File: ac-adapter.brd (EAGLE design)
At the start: 113 x 52.7 mm, 88 parts, among them IC1 SSC3S900, IC2 TL431, Q1 300V 5A, Q2 300V 5A, Q3 TLP621-1, T1 COMMON_FILTER-SU10VFC, T2 TRANSFORMAER_FLYBACK-ETD34

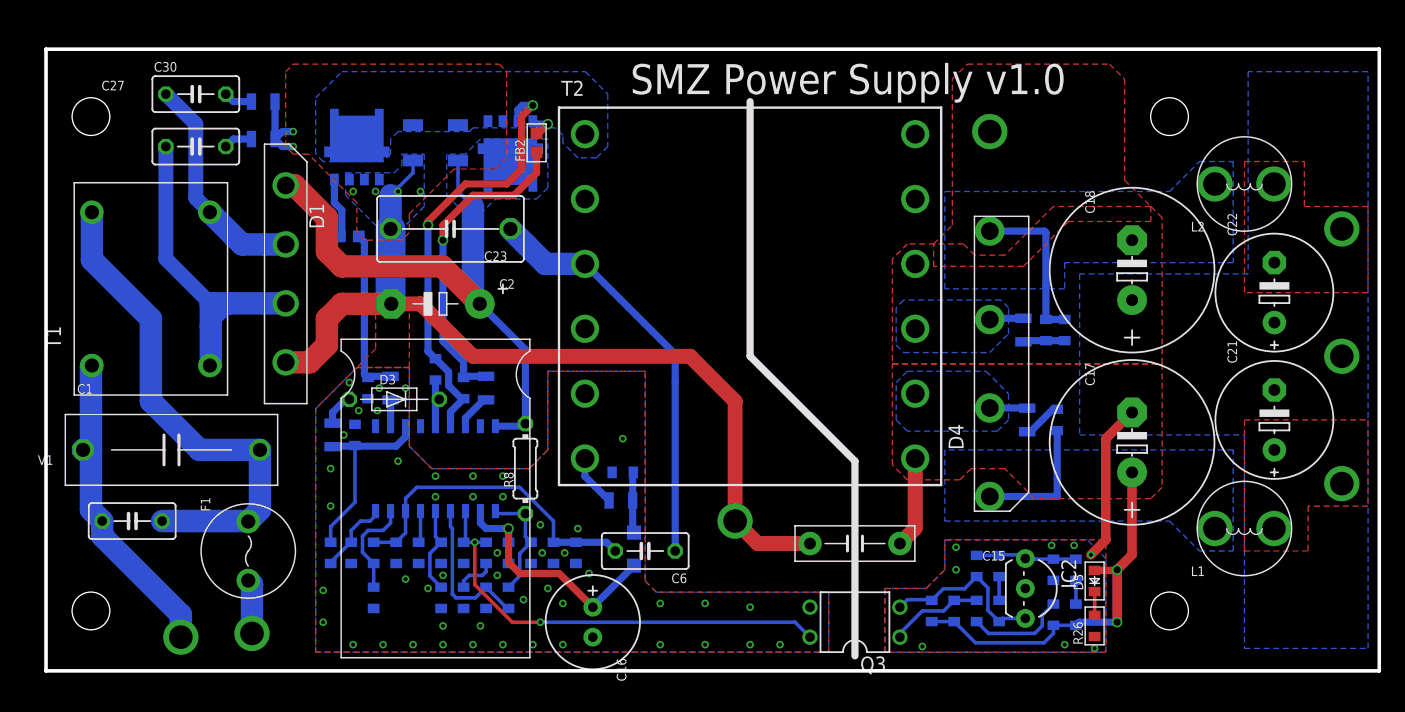
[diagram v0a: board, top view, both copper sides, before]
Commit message: GaNに変更
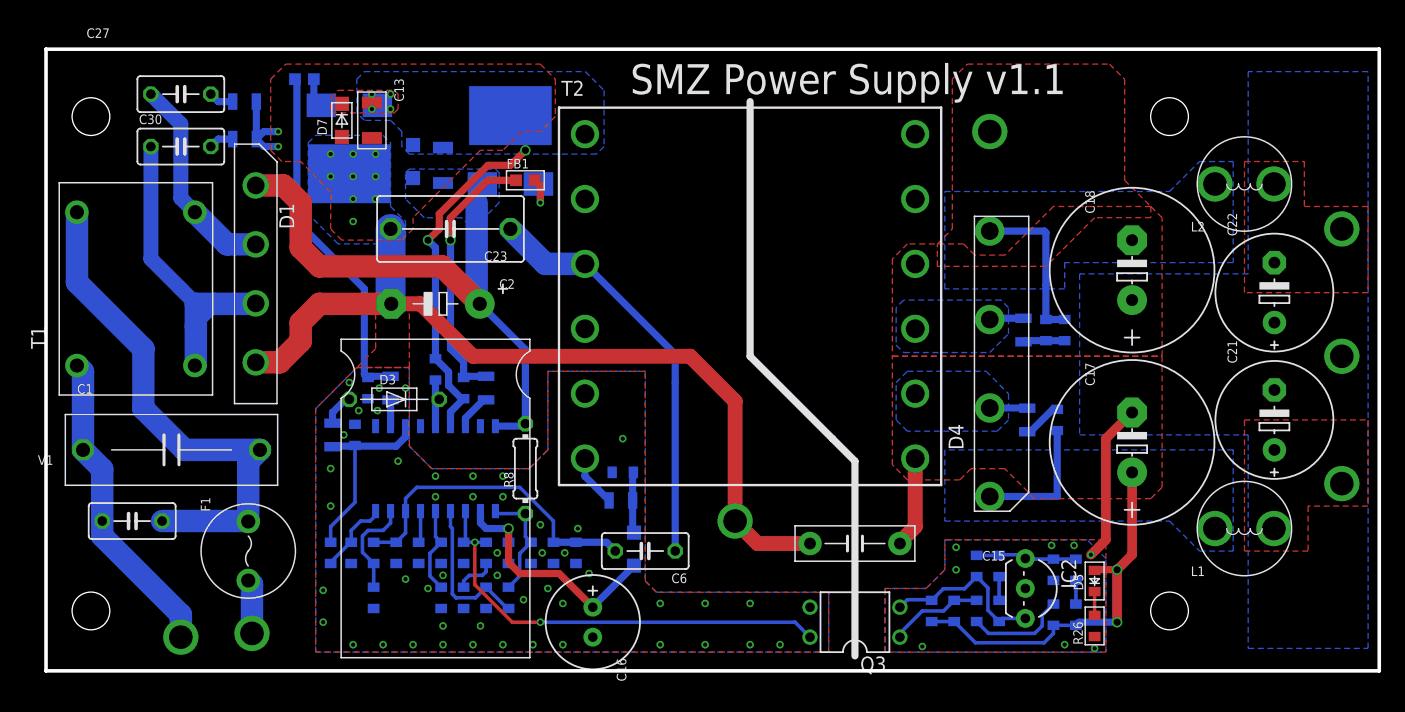
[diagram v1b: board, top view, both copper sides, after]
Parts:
- added D6, D7: SBD-1A2, my_rcl:SOD123
- Q1, Q2: device my_ic:DFN5_5X6 -> my_ic:PQFN8X8
- moved FB2 20.4 mm to (21.9, 50.2), flipped to the bottom, turned to 180 degrees
- moved FB1 15.7 mm to (40.6, 41.6), flipped to the top
- moved C27 4.62 mm to (11.4, 48.9)
- moved C30 4.62 mm to (11.4, 44.5)
- moved C13 3.98 mm to (27.6, 46.7), flipped to the top
- moved Q2 3.55 mm to (25.7, 47.9)
- moved R28 3.55 mm to (16.8, 48.3)
- moved R29 3.55 mm to (16.8, 45.1)
- moved D1 2.54 mm to (17.8, 33.7)
- moved Q1 2.54 mm to (39.4, 41.3)
- moved C29 2.29 mm to (33.7, 42.9)
- moved T1 1.27 mm to (7.62, 32.4)
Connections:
- net N$2: now also FB1.1; no longer FB2.1
- net N$39: now also Q1.G; no longer Q2.4
- net N$4: now also C30.1; no longer C27.1
- net N$41: now also Q2.G; no longer Q1.4
- net N$5: now also C27.1; no longer C30.1
- net N$9: now also FB2.1; no longer FB1.1
- net PGND: now also D7.1, Q2.S; no longer Q2.1, Q2.2, Q2.3
- net SW: now also D6.1, D7.2, Q1.S, Q2.D; no longer Q1.1, Q1.2, Q1.3, Q2.5_6, Q2.5_6_1, Q2.5_6_2, Q2.5_6_3, Q2.5_6_4
- net VH: now also D6.2, Q1.D; no longer Q1.5_6, Q1.5_6_1, Q1.5_6_2, Q1.5_6_3, Q1.5_6_4
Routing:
- net N$9: track 14.3 -> 29.8 mm
- net SW: track 37.1 -> 29.7 mm, vias 2 -> 6
- net N$2: track 27.1 -> 22.8 mm
- net PGND: track 81.9 -> 78.1 mm, vias 54 -> 59
- net N$39: track 5.16 -> 3.76 mm, vias 0 -> 1
- net N$4: track 29.1 -> 27.8 mm
- net N$5: track 19.1 -> 17.8 mm
- net N$26: track 42.9 -> 44.1 mm
- net VH: track 49.6 -> 48.4 mm
- net N$41: track 2.65 -> 2.49 mm, vias 1 -> 0
- added copper zone on layer 1, net SW
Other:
- board text added: "SMZ Power Supply v1.1"
- board text removed: "SMZ Power Supply v1.0"
